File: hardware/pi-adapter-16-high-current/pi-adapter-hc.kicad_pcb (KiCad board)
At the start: 4 copper layers, 64 x 56 mm, 38 parts, among them J1 Conn_02x02_Odd_Even, P1 CONN_01X04, P10 CONN_01X04, P11 CONN_01X04, P12 CONN_01X04, P13 CONN_01X04, P14 CONN_01X04, P15 CONN_01X04, P16 CONN_01X04, P17 5V, P2 CONN_01X04, P20 CONN_02X20, P21 I2C, P22 System SPI, P23 UART, P3 CONN_01X04, P30 +5V, P31 GND, P4 CONN_01X04, P40 CONN_01X01, P41 CONN_01X01, P43 CONN_01X01, P5 CONN_01X04, P6 CONN_01X04, P7 CONN_01X04, P8 CONN_01X04, P9 CONN_01X04, U1 74AHCT245, U2 74AHCT245, U3 74AHCT245, U4 74AHCT245

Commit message: Update to latest version of KiCAD
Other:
- net class Default removed
- net class power removed

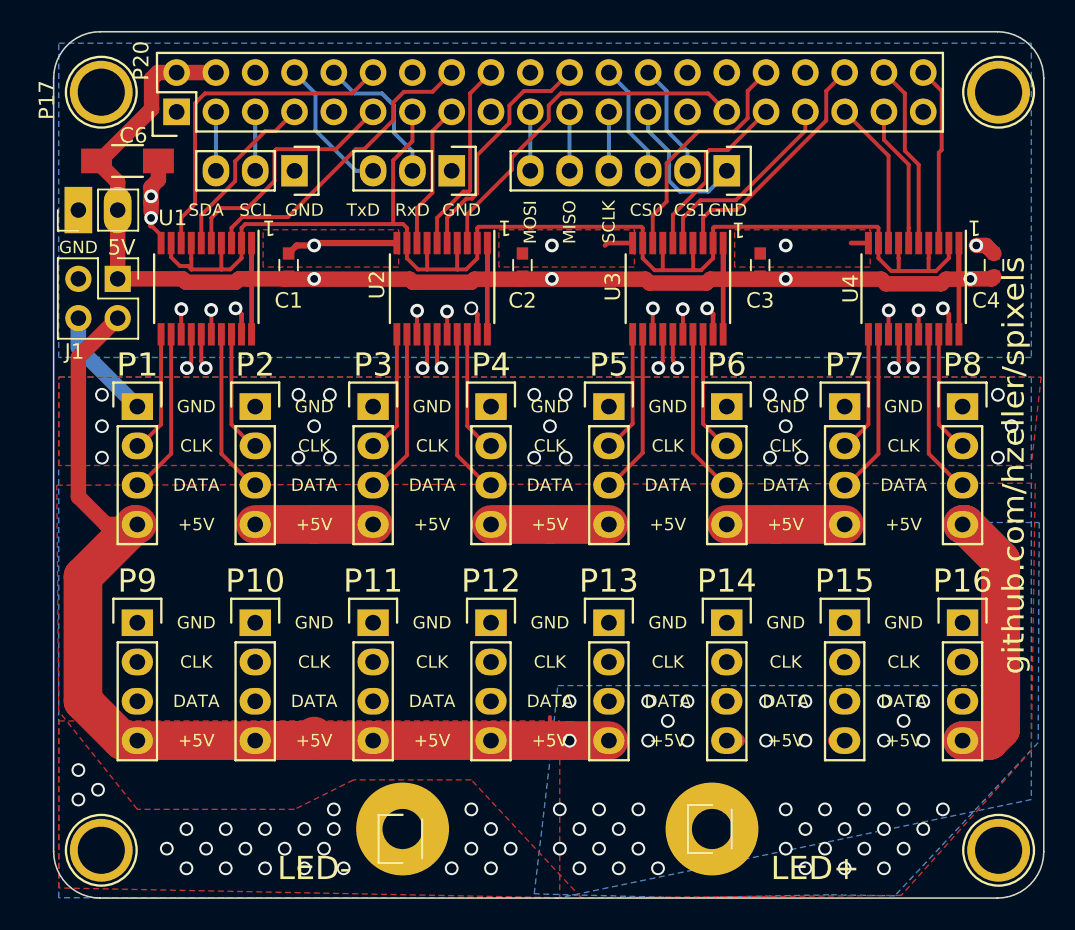
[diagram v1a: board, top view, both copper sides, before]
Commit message: Update symbols and packages.
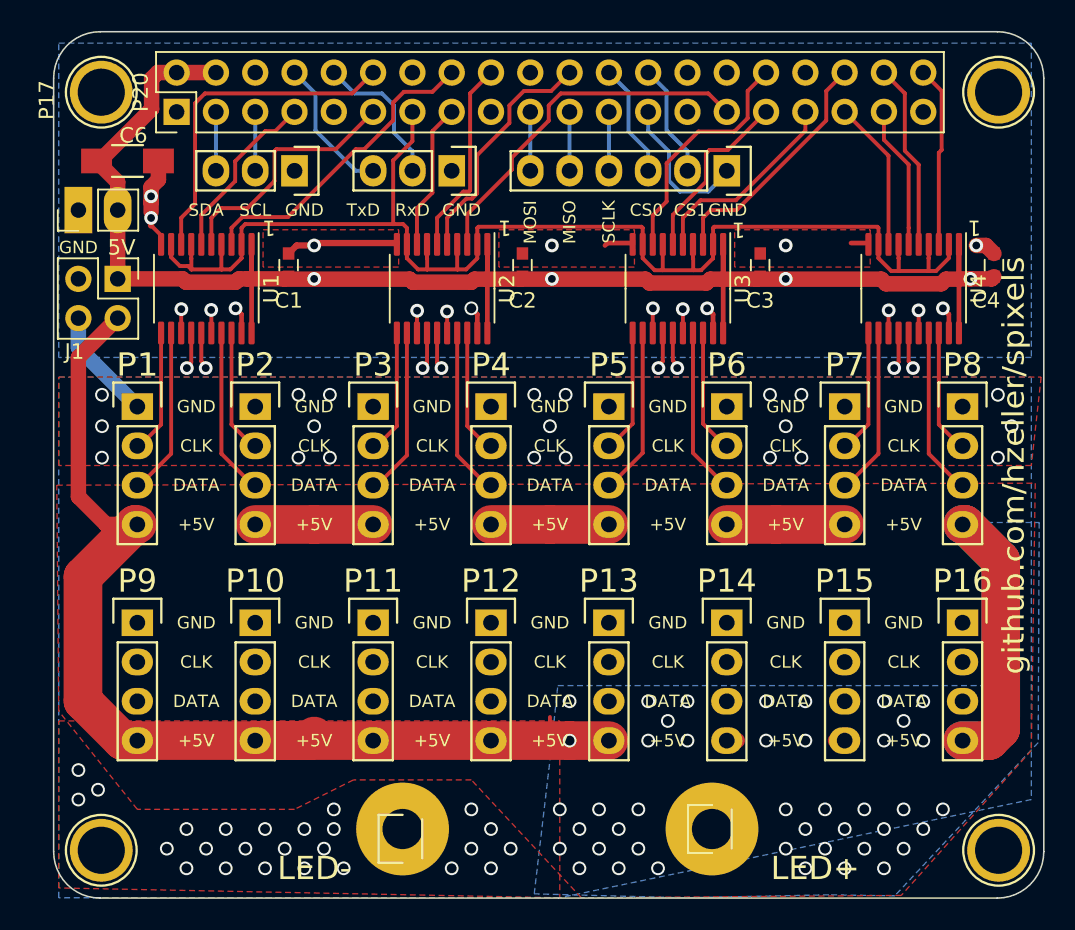
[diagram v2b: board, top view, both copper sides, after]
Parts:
- P20: value CONN_02X20 -> Pi-GPIO; footprint Pin_Headers:Pin_Header_Straight_2x20 -> Connector_PinHeader_2.54mm:PinHeader_2x20_P2.54mm_Vertical
- U1, U2, U3, U4: value 74AHCT245 -> 74HC245; footprint Housings_SSOP:TSSOP-20_4.4x6.5mm_Pitch0.65mm -> Package_SO:TSSOP-20_4.4x6.5mm_P0.65mm
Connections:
- net Net-(P20-Pad1) renamed no_connect_63
- net Net-(P20-Pad17) renamed no_connect_64
- net Net-(P20-Pad27) renamed no_connect_65
- net Net-(P20-Pad28) renamed no_connect_66
- net Net-(P20-Pad9) renamed no_connect_67
